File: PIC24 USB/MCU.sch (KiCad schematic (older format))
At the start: 8 parts, among them U1 PIC24FJXXXGB106

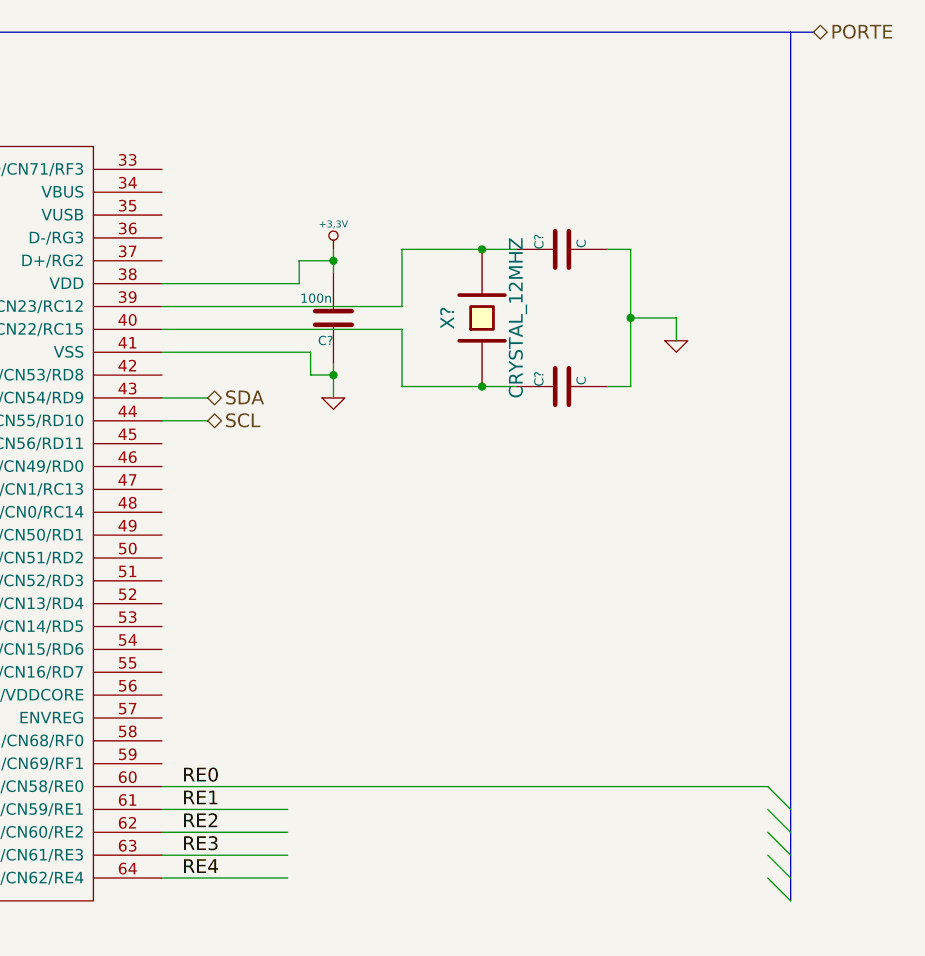
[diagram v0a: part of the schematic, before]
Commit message: Connected ENVREG and placed VDDCORE capacitor for pic24 version
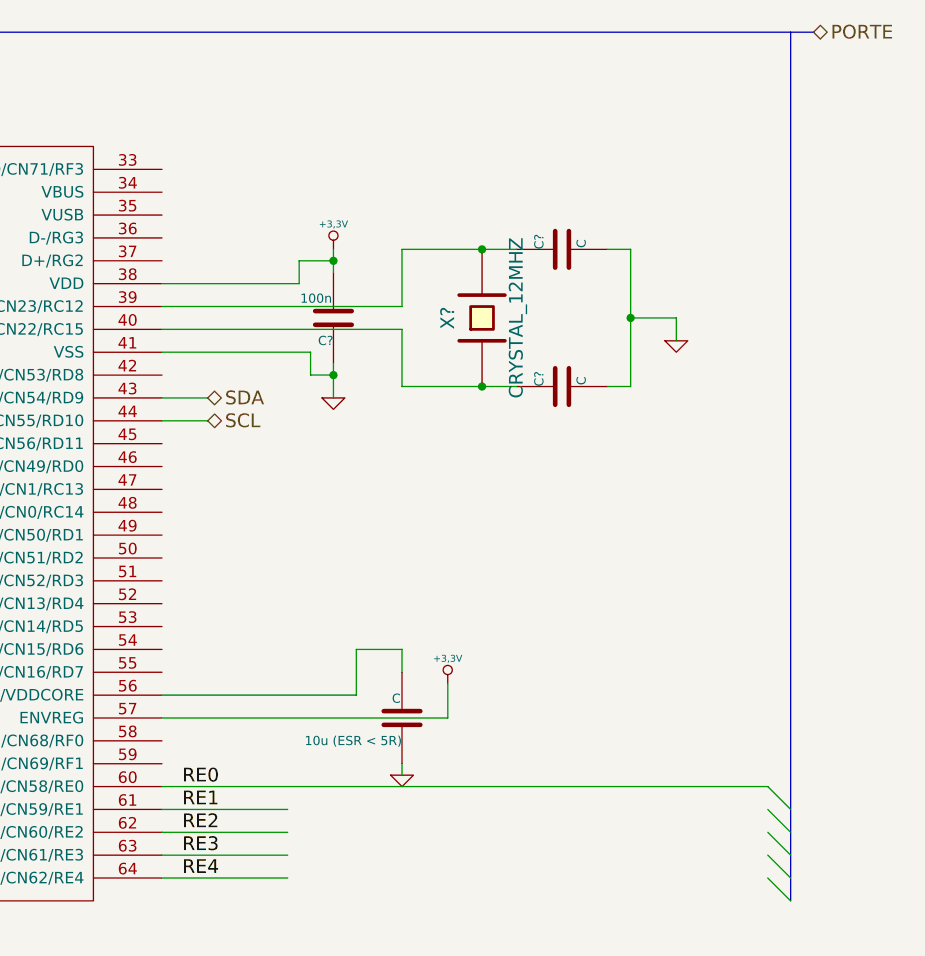
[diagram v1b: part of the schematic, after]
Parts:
- added 10u: C, ~, symbol C
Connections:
- wire segments 54 -> 61
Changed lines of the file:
@@
-EESchema Schematic File Version 2  date 31.07.2014 14:53:53
+EESchema Schematic File Version 2  date 01.08.2014 22:56:17
 LIBS:power
 LIBS:device
@@
 LIBS:CircuitHub
 LIBS:microchip_hele
+LIBS:PIC24_USB_IR_Transmitter-cache
 EELAYER 27 0
 EELAYER END
@@
 Sheet 2 2
 Title ""
-Date "31 jul 2014"
+Date "1 aug 2014"
 Rev ""
 Comp ""
@@
 	9950 5000 10050 5100
 Wire Bus Line
-	10050 5500 10050 1700
+	10050 1700 10050 5500
 Entry Wire Line
 	2550 2200 2650 2300
@@
 Text Label 7550 5400 2    60   ~ 0
 RE4
+$Comp
+L +3,3V #PWR?
+U 1 1 53DBFFDE
+P 8550 4550
+F 0 "#PWR?" H 8550 4510 30  0001 C CNN
+F 1 "+3,3V" H 8550 4660 30  0000 C CNN
+F 2 "" H 8550 4550 60  0000 C CNN
+F 3 "" H 8550 4550 60  0000 C CNN
+	1    8550 4550
+	1    0    0    -1
+$EndComp
+Wire Wire Line
+	7300 4700 8550 4700
+Wire Wire Line
+	8550 4700 8550 4550
+Wire Wire Line
+	7300 4600 8150 4600
+Wire Wire Line
+	8150 4400 8350 4400
+$Comp
+L C 10u
+U 1 1 53DC00CE
+P 8350 4700
+F 0 "10u (ESR < 5R)" H 8350 4800 40  0000 L CNN
+F 1 "C" H 8356 4615 40  0000 L CNN
+F 2 "~" H 8388 4550 30  0000 C CNN
+F 3 "~" H 8350 4700 60  0000 C CNN
+	1    8350 4700
+	-1   0    0    1
+$EndComp
+Wire Wire Line
+	8350 4400 8350 4500
+$Comp
+L GND #PWR?
+U 1 1 53DC0153
+P 8350 4950
+F 0 "#PWR?" H 8350 4950 30  0001 C CNN
+F 1 "GND" H 8350 4880 30  0001 C CNN
+F 2 "" H 8350 4950 60  0000 C CNN
+F 3 "" H 8350 4950 60  0000 C CNN
+	1    8350 4950
+	1    0    0    -1
+$EndComp
+Wire Wire Line
+	8350 4900 8350 4950
+Wire Wire Line
+	8150 4600 8150 4400
 $EndSCHEMATC

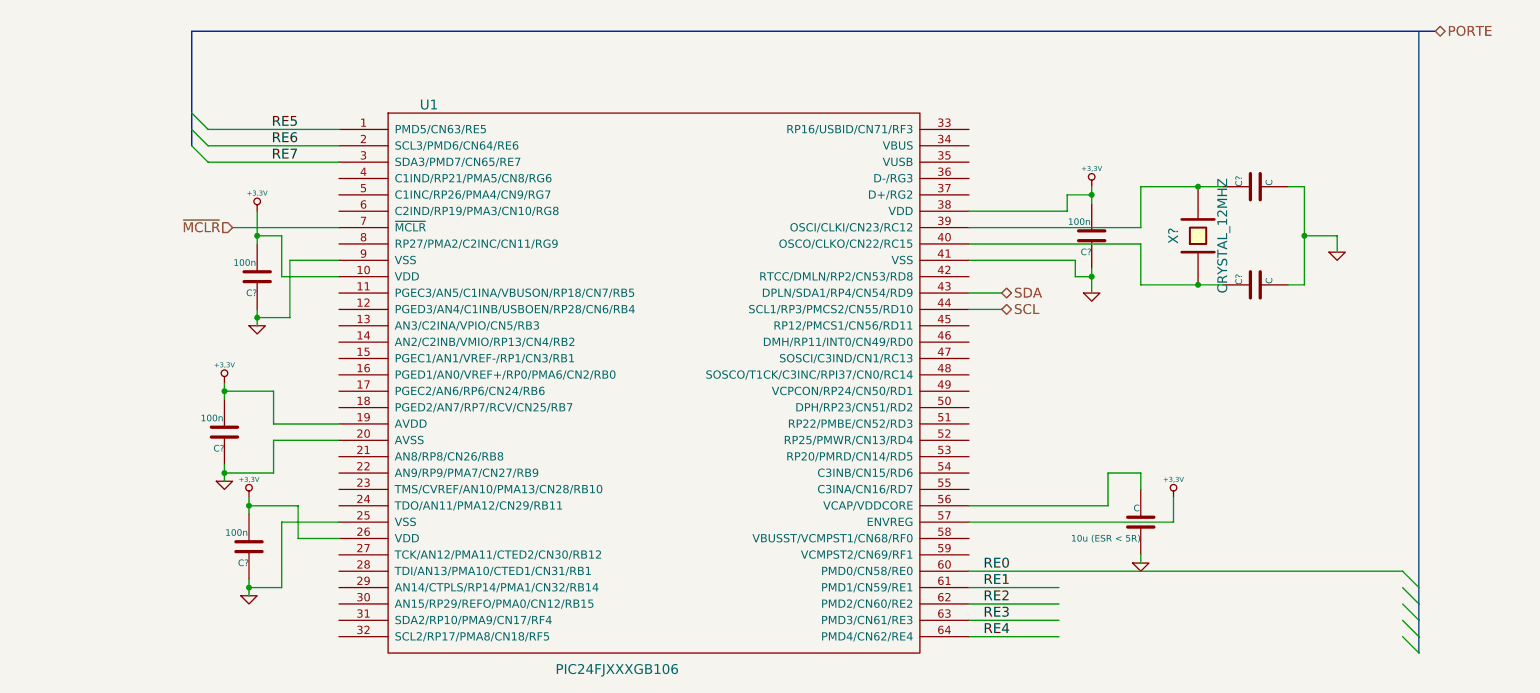
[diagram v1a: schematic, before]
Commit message: inserted some mandatory mcu connecrtion and a bus connection
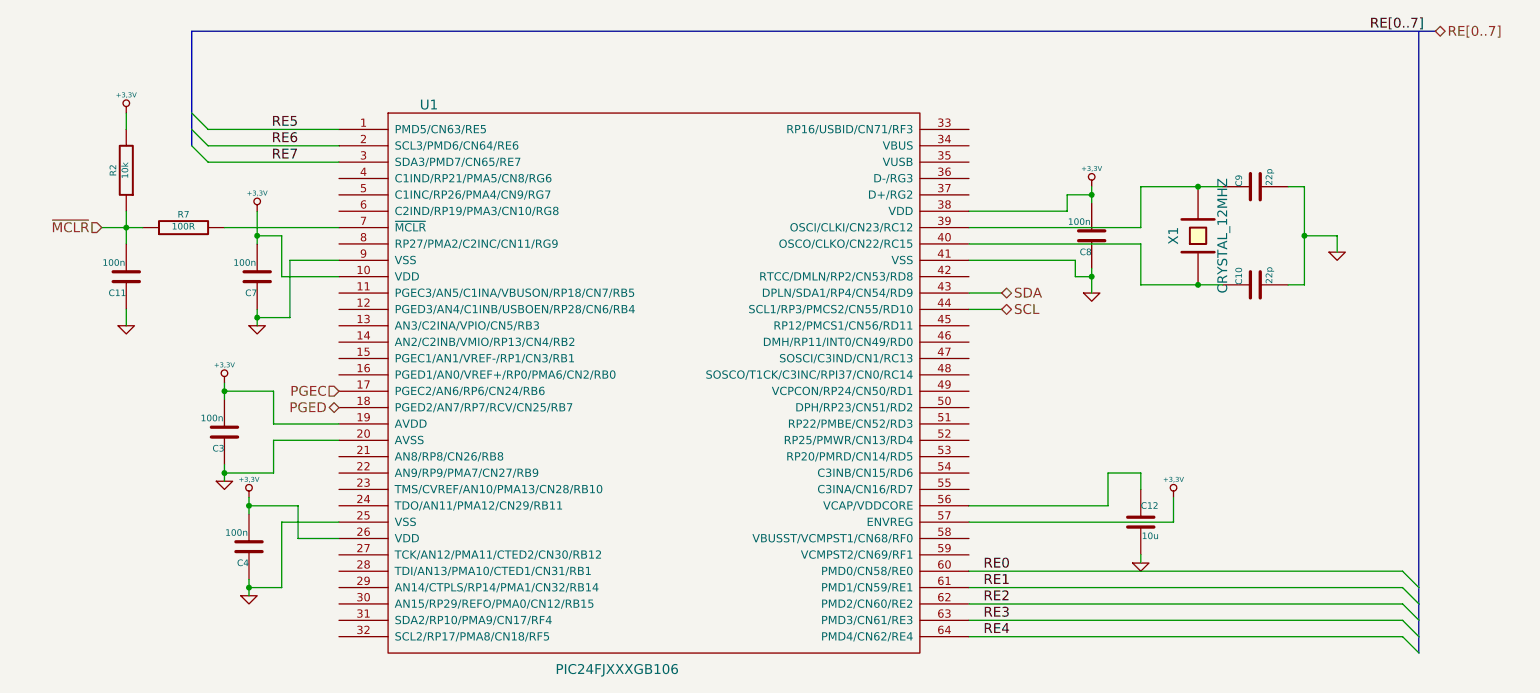
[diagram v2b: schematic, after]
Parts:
- added C11: 100n, ~, symbol C
- added R2: 10k, ~, symbol R
- added R7: 100R, ~, symbol R
- C10, C9: renamed from C?; value C -> 22p
- C12: renamed from 10u; value C -> 10u
- gave numbers to parts that had none: 5
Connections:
- net labels added: PGEC, PGED, RE[0..7]
- net labels removed: PORTE
- wire segments 61 -> 65
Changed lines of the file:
@@
-EESchema Schematic File Version 2  date 01.08.2014 22:56:17
+EESchema Schematic File Version 2  date 03.08.2014 21:39:24
 LIBS:power
 LIBS:device
@@
 Sheet 2 2
 Title ""
-Date "1 aug 2014"
+Date "3 aug 2014"
 Rev ""
 Comp ""
@@
 Comment4 ""
 $EndDescr
-Text HLabel 2800 2900 0    60   Input ~ 0
+Text HLabel 2000 2900 0    60   Input ~ 0
 ~MCLR
 $Comp
-L GND #PWR032
+L GND #PWR034
 U 1 1 53DA26E1
 P 2950 3500
-F 0 "#PWR032" H 2950 3500 30  0001 C CNN
+F 0 "#PWR034" H 2950 3500 30  0001 C CNN
 F 1 "GND" H 2950 3430 30  0001 C CNN
 F 2 "" H 2950 3500 60  0000 C CNN
@@
 $EndComp
 $Comp
-L GND #PWR033
+L GND #PWR035
 U 1 1 53DA26EE
 P 2900 5150
-F 0 "#PWR033" H 2900 5150 30  0001 C CNN
+F 0 "#PWR035" H 2900 5150 30  0001 C CNN
 F 1 "GND" H 2900 5080 30  0001 C CNN
 F 2 "" H 2900 5150 60  0000 C CNN
@@
 $EndComp
 $Comp
-L GND #PWR034
+L GND #PWR036
 U 1 1 53DA26F4
 P 8050 3300
-F 0 "#PWR034" H 8050 3300 30  0001 C CNN
+F 0 "#PWR036" H 8050 3300 30  0001 C CNN
 F 1 "GND" H 8050 3230 30  0001 C CNN
 F 2 "" H 8050 3300 60  0000 C CNN
@@
 $EndComp
 $Comp
-L PIC24FJXXXGB106 U1
-U 1 1 53DA2811
-P 4550 2100
-F 0 "U1" H 4000 2050 60  0000 C CNN
-F 1 "PIC24FJXXXGB106" H 5150 -1400 60  0000 C CNN
-F 2 "~" H 4550 2100 60  0000 C CNN
-F 3 "~" H 4550 2100 60  0000 C CNN
-	1    4550 2100
-	1    0    0    -1
-$EndComp
-$Comp
-L +3,3V #PWR035
+L +3,3V #PWR037
 U 1 1 53DA2840
 P 8050 2650
-F 0 "#PWR035" H 8050 2610 30  0001 C CNN
+F 0 "#PWR037" H 8050 2610 30  0001 C CNN
 F 1 "+3,3V" H 8050 2760 30  0000 C CNN
 F 2 "" H 8050 2650 60  0000 C CNN
@@
 $EndComp
 $Comp
-L +3,3V #PWR036
+L +3,3V #PWR038
 U 1 1 53DA284D
 P 2950 2800
-F 0 "#PWR036" H 2950 2760 30  0001 C CNN
+F 0 "#PWR038" H 2950 2760 30  0001 C CNN
 F 1 "+3,3V" H 2950 2910 30  0000 C CNN
 F 2 "" H 2950 2800 60  0000 C CNN
@@
 $EndComp
 $Comp
-L +3,3V #PWR037
+L +3,3V #PWR039
 U 1 1 53DA2853
 P 2900 4550
-F 0 "#PWR037" H 2900 4510 30  0001 C CNN
+F 0 "#PWR039" H 2900 4510 30  0001 C CNN
 F 1 "+3,3V" H 2900 4660 30  0000 C CNN
 F 2 "" H 2900 4550 60  0000 C CNN
@@
 $EndComp
 $Comp
-L +3,3V #PWR039
+L +3,3V #PWR040
 U 1 1 53DA2865
 P 2750 3850
-F 0 "#PWR039" H 2750 3810 30  0001 C CNN
+F 0 "#PWR040" H 2750 3810 30  0001 C CNN
 F 1 "+3,3V" H 2750 3960 30  0000 C CNN
 F 2 "" H 2750 3850 60  0000 C CNN
@@
 $EndComp
 $Comp
-L CRYSTAL X?
+L CRYSTAL X1
 U 1 1 53DA32F3
 P 8700 2950
-F 0 "X?" H 8700 3100 60  0000 C CNN
+F 0 "X1" H 8700 3100 60  0000 C CNN
 F 1 "CRYSTAL_12MHZ" H 8700 2800 60  0000 C CNN
 F 2 "~" H 8700 2950 60  0000 C CNN
@@
 $EndComp
 $Comp
-L C C?
+L C C9
 U 1 1 53DA330C
 P 9050 2650
-F 0 "C?" H 9050 2750 40  0000 L CNN
-F 1 "C" H 9056 2565 40  0000 L CNN
+F 0 "C9" H 9050 2750 40  0000 L CNN
+F 1 "22p" H 9056 2565 40  0000 L CNN
 F 2 "~" H 9088 2500 30  0000 C CNN
 F 3 "~" H 9050 2650 60  0000 C CNN
@@
 $EndComp
 $Comp
-L C C?
+L C C10
 U 1 1 53DA3319
 P 9050 3250
-F 0 "C?" H 9050 3350 40  0000 L CNN
-F 1 "C" H 9056 3165 40  0000 L CNN
+F 0 "C10" H 9050 3350 40  0000 L CNN
+F 1 "22p" H 9056 3165 40  0000 L CNN
 F 2 "~" H 9088 3100 30  0000 C CNN
 F 3 "~" H 9050 3250 60  0000 C CNN
@@
 $EndComp
 $Comp
-L GND #PWR?
+L GND #PWR041
 U 1 1 53DA331F
 P 9550 3050
-F 0 "#PWR?" H 9550 3050 30  0001 C CNN
+F 0 "#PWR041" H 9550 3050 30  0001 C CNN
 F 1 "GND" H 9550 2980 30  0001 C CNN
 F 2 "" H 9550 3050 60  0000 C CNN
@@
 $EndComp
 Wire Wire Line
-	3450 2900 2800 2900
-Wire Wire Line
 	3450 3100 3150 3100
 Wire Wire Line
@@
 Connection ~ 8700 2650
 $Comp
-L C C?
+L C C3
 U 1 1 53DA3435
 P 2750 4150
-F 0 "C?" H 2750 4250 40  0000 L CNN
+F 0 "C3" H 2750 4250 40  0000 L CNN
 F 1 "100n" H 2756 4065 40  0000 L CNN
 F 2 "~" H 2788 4000 30  0000 C CNN
@@
 $EndComp
 $Comp
-L GND #PWR?
+L GND #PWR042
 U 1 1 53DA3460
 P 2750 4450
-F 0 "#PWR?" H 2750 4450 30  0001 C CNN
+F 0 "#PWR042" H 2750 4450 30  0001 C CNN
 F 1 "GND" H 2750 4380 30  0001 C CNN
 F 2 "" H 2750 4450 60  0000 C CNN
@@
 Connection ~ 2750 4400
 $Comp
-L C C?
+L C C4
 U 1 1 53DA3506
 P 2900 4850
-F 0 "C?" H 2900 4950 40  0000 L CNN
+F 0 "C4" H 2900 4950 40  0000 L CNN
 F 1 "100n" H 2906 4765 40  0000 L CNN
 F 2 "~" H 2938 4700 30  0000 C CNN
@@
 Connection ~ 2900 5100
 $Comp
-L C C?
+L C C7
 U 1 1 53DA35D7
 P 2950 3200
-F 0 "C?" H 2950 3300 40  0000 L CNN
+F 0 "C7" H 2950 3300 40  0000 L CNN
 F 1 "100n" H 2956 3115 40  0000 L CNN
 F 2 "~" H 2988 3050 30  0000 C CNN
@@
 Connection ~ 2950 3450
 $Comp
-L C C?
+L C C8
 U 1 1 53DA3748
 P 8050 2950
-F 0 "C?" H 8050 3050 40  0000 L CNN
+F 0 "C8" H 8050 3050 40  0000 L CNN
 F 1 "100n" H 8056 2865 40  0000 L CNN
 F 2 "~" H 8088 2800 30  0000 C CNN
@@
 RE7
 Text HLabel 10150 1700 2    60   BiDi ~ 0
-PORTE
+RE[0..7]
 Wire Wire Line
 	7300 5000 9950 5000
 Wire Wire Line
-	7300 5100 7850 5100
-Wire Wire Line
-	7300 5200 7850 5200
-Wire Wire Line
-	7300 5300 7850 5300
-Wire Wire Line
-	7300 5400 7850 5400
+	7300 5200 9950 5200
+Wire Wire Line
+	7300 5300 9950 5300
+Wire Wire Line
+	7300 5400 9950 5400
 Text Label 7550 5000 2    60   ~ 0
 RE0
@@
 RE4
 $Comp
-L +3,3V #PWR?
+L +3,3V #PWR043
 U 1 1 53DBFFDE
 P 8550 4550
-F 0 "#PWR?" H 8550 4510 30  0001 C CNN
+F 0 "#PWR043" H 8550 4510 30  0001 C CNN
 F 1 "+3,3V" H 8550 4660 30  0000 C CNN
 F 2 "" H 8550 4550 60  0000 C CNN
@@
 	8150 4400 8350 4400
 $Comp
-L C 10u
+L C C12
 U 1 1 53DC00CE
 P 8350 4700
-F 0 "10u (ESR < 5R)" H 8350 4800 40  0000 L CNN
-F 1 "C" H 8356 4615 40  0000 L CNN
+F 0 "C12" H 8350 4800 40  0000 L CNN
+F 1 "10u" H 8356 4615 40  0000 L CNN
 F 2 "~" H 8388 4550 30  0000 C CNN
 F 3 "~" H 8350 4700 60  0000 C CNN
 	1    8350 4700
-	-1   0    0    1
+	1    0    0    -1
 $EndComp
 Wire Wire Line
 	8350 4400 8350 4500
 $Comp
-L GND #PWR?
+L GND #PWR044
 U 1 1 53DC0153
 P 8350 4950
-F 0 "#PWR?" H 8350 4950 30  0001 C CNN
+F 0 "#PWR044" H 8350 4950 30  0001 C CNN
 F 1 "GND" H 8350 4880 30  0001 C CNN
 F 2 "" H 8350 4950 60  0000 C CNN
@@
 Wire Wire Line
 	8150 4600 8150 4400
+Wire Wire Line
+	7300 5100 9950 5100
+$Comp
+L PIC24FJXXXGB106 U1
+U 1 1 53DA2811
+P 4550 2100
+F 0 "U1" H 4000 2050 60  0000 C CNN
+F 1 "PIC24FJXXXGB106" H 5150 -1400 60  0000 C CNN
+F 2 "~" H 4550 2100 60  0000 C CNN
+F 3 "~" H 4550 2100 60  0000 C CNN
+	1    4550 2100
+	1    0    0    -1
+$EndComp
+Text HLabel 3450 3900 0    60   Input ~ 0
+PGEC
+Text HLabel 3450 4000 0    60   BiDi ~ 0
+PGED
+$Comp
+L R R7
+U 1 1 53DEB244
+P 2500 2900
+F 0 "R7" V 2580 2900 40  0000 C CNN
+F 1 "100R" V 2507 2901 40  0000 C CNN
+F 2 "~" V 2430 2900 30  0000 C CNN
+F 3 "~" H 2500 2900 30  0000 C CNN
+	1    2500 2900
+	0    -1   -1   0
+$EndComp
+$Comp
+L R R2
+U 1 1 53DEB251
+P 2150 2550
+F 0 "R2" V 2230 2550 40  0000 C CNN
+F 1 "10k" V 2157 2551 40  0000 C CNN
+F 2 "~" V 2080 2550 30  0000 C CNN
+F 3 "~" H 2150 2550 30  0000 C CNN
+	1    2150 2550
+	-1   0    0    1
+$EndComp
+$Comp
+L C C11
+U 1 1 53DEB257
+P 2150 3200
+F 0 "C11" H 2150 3300 40  0000 L CNN
+F 1 "100n" H 2156 3115 40  0000 L CNN
+F 2 "~" H 2188 3050 30  0000 C CNN
+F 3 "~" H 2150 3200 60  0000 C CNN
+	1    2150 3200
+	-1   0    0    1
+$EndComp
+$Comp
+L GND #PWR045
+U 1 1 53DEB25D
+P 2150 3500
+F 0 "#PWR045" H 2150 3500 30  0001 C CNN
+F 1 "GND" H 2150 3430 30  0001 C CNN
+F 2 "" H 2150 3500 60  0000 C CNN
+F 3 "" H 2150 3500 60  0000 C CNN
+	1    2150 3500
+	1    0    0    -1
+$EndComp
+$Comp
+L +3,3V #PWR046
+U 1 1 53DEB263
+P 2150 2200
+F 0 "#PWR046" H 2150 2160 30  0001 C CNN
+F 1 "+3,3V" H 2150 2310 30  0000 C CNN
+F 2 "" H 2150 2200 60  0000 C CNN
+F 3 "" H 2150 2200 60  0000 C CNN
+	1    2150 2200
+	1    0    0    -1
+$EndComp
+Wire Wire Line
+	3450 2900 2750 2900
+Wire Wire Line
+	2250 2900 2000 2900
+Wire Wire Line
+	2150 3000 2150 2800
+Connection ~ 2150 2900
+Wire Wire Line
+	2150 3400 2150 3500
+Wire Wire Line
+	2150 2200 2150 2300
+Text Label 9750 1700 0    60   ~ 0
+RE[0..7]
 $EndSCHEMATC
